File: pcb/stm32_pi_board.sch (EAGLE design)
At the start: 96 parts, among them IC1 MIC5219-3.3, IC2 ESP-11, IC3 IS31AP2005, IC4 STM32F405RG, IC5 STF203-22, IC6 MIC5219-3.3, IC7 IS31AP2005, IC8 MIC5219-3.3, IC9 UDA1334ATS, Q1 FDG6332C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

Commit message: New version of pi_board
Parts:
- removed ESPJ2: LSP10, MyComponents:LSP10
- removed IC1: MIC5219-3.3, MyComponents:MIC5219XX
- removed SV2: 75867-331LF, MyComponents:MA03-2
- added C38: 0.1uF, MyComponents:C-US0805
- added GN-RX-TX: (no value), MyComponents:MA03-1PL
- added IC10: REG1117, MyComponents:REG1117
- added L3: 1 uH, MyComponents:L-USL0805
- added R26, R27: 330, MyComponents:R-US0805
- added R28: 1, MyComponents:R-US0805
- C6: value 470pF -> 100 uF; device MyComponents:C-US0805 -> MyComponents:CPOL-US1311
- C7: value 2.2uF -> 47 uF
- D1: value WP154A4SUREQBFZGC -> (none); device MyComponents:RGB-LED-5MM -> MyComponents:RGB-LED3X1MM
- FLASH: value LSP10 -> (none); device MyComponents:LSP10 -> MyComponents:MA02-1
- HSE: device MyComponents:Q-HSEFA-128 -> MyComponents:Q-HSEHC-46X
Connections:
- removed net D1_BLUE: D1.AB, IC4MCU.PC2
- removed net D1_GREEN: D1.AG, IC4MCU.PC1
- removed net D1_RED: D1.AR, IC4MCU.PC3
- new net N$75: D1.AR, R27.1
- new net N$85: IC10.VOUT, R28.2
- new net N$90: L3.1, R28.1
- new net PC1: IC4MCU.PC1, SV3.6
- new net PC2: IC4MCU.PC2, SV3.5
- new net PC3: IC4MCU.PC3, SV3.4
- net ESP-IO0: now also FLASH.1; no longer FLASH.MP
- net ESP-RXI: now also GN-RX-TX.2; no longer SV2.5
- net ESP-TXI: now also GN-RX-TX.3; no longer SV2.3
- net GND: now also C38.2, C6.-, D1.C, FLASH.2, GN-RX-TX.1, IC10.GND; no longer C6.1, ESPJ2.MP, IC1.GND, R6.2, SV2.1
- net N$40: now also D1.AB, R26.1; no longer D1.C, R6.1
- net N$5: now also D1.AG, R6.1; no longer C6.2, IC1.BYP
- net PB4: now also R27.2; no longer SV3.11
- net PB5: now also R26.2; no longer SV3.10
- net PB6: now also SV3.11; no longer SV3.9
- net PB7: now also SV3.10; no longer SV3.8
- net PB8: now also R6.2; no longer SV3.7
- net PB9: now also SV3.9; no longer SV3.6
- net PC0: now also SV3.7; no longer SV3.4
- net PC13: now also SV3.8; no longer SV3.5
- net VDD: now also C6.+, L3.2; no longer IC1.OUT
- net VIN: now also C38.1, IC10.VIN; no longer IC1.EN, IC1.IN
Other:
- moved on the sheet: C10, C11, C12, C13, C14, C2, C3, C7, C8, C9, D1, ESP-ON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

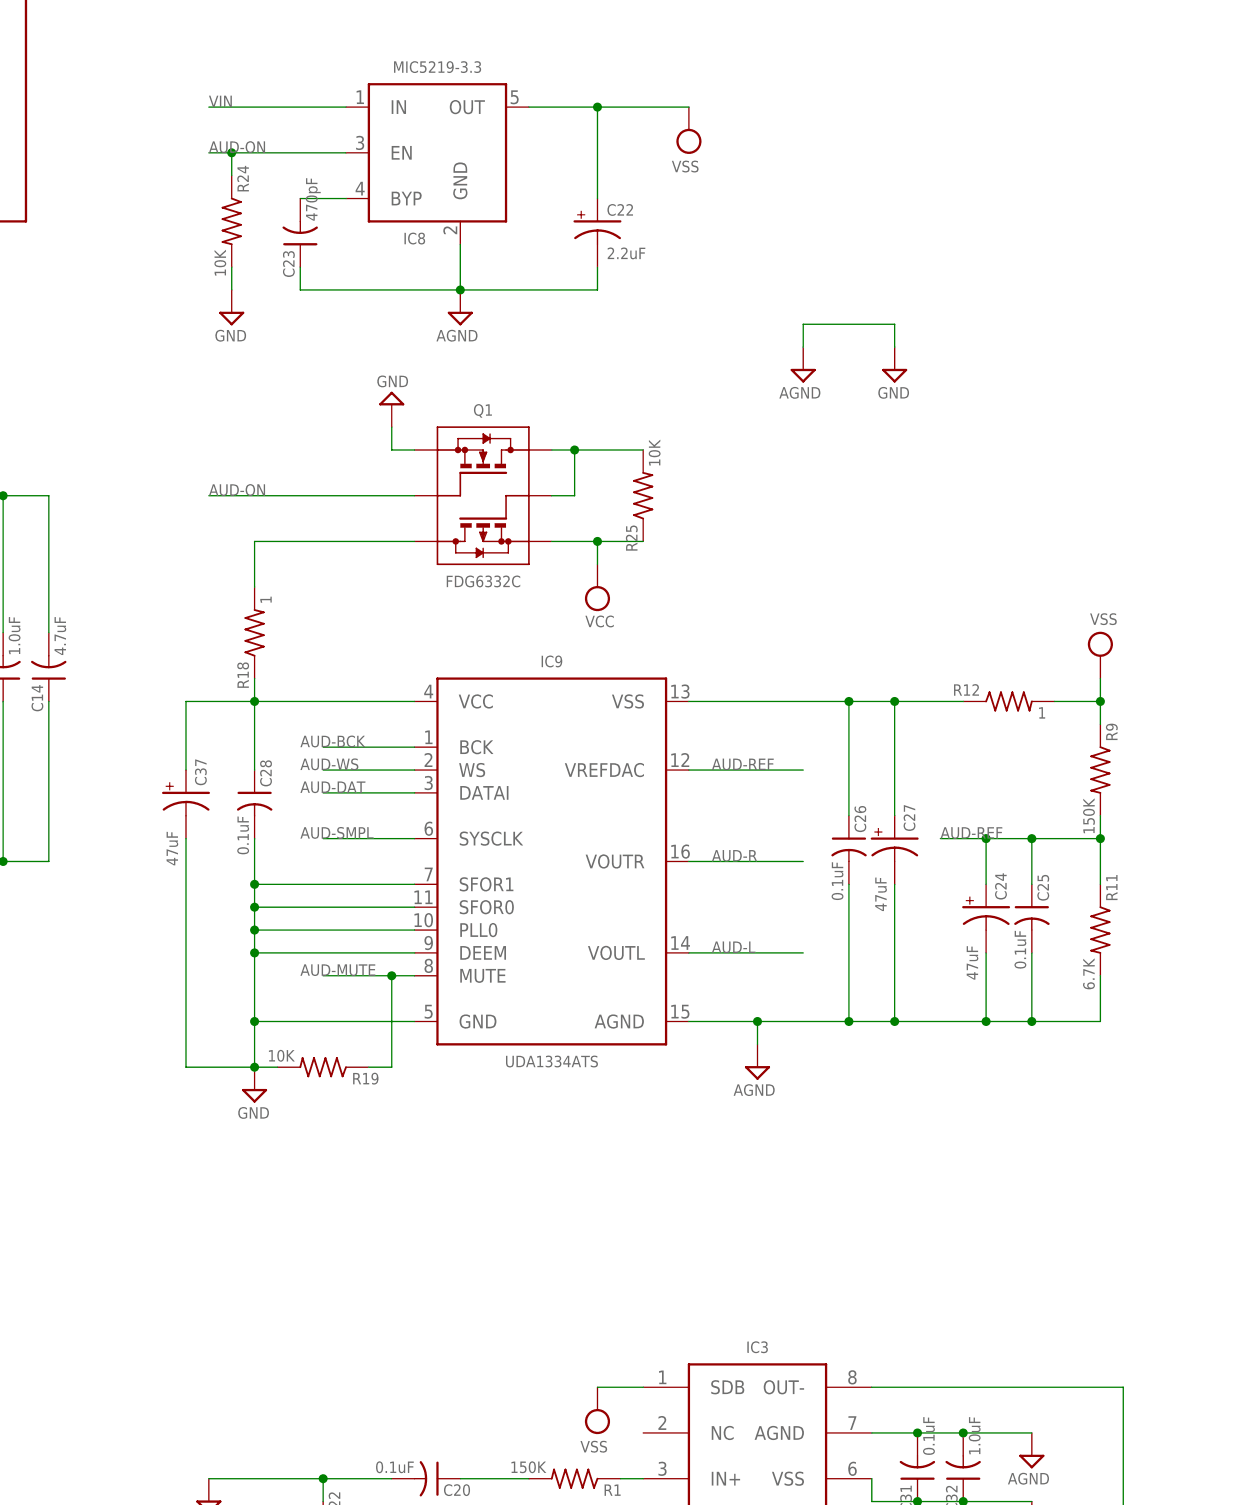
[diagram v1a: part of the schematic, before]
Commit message: Added LMT86
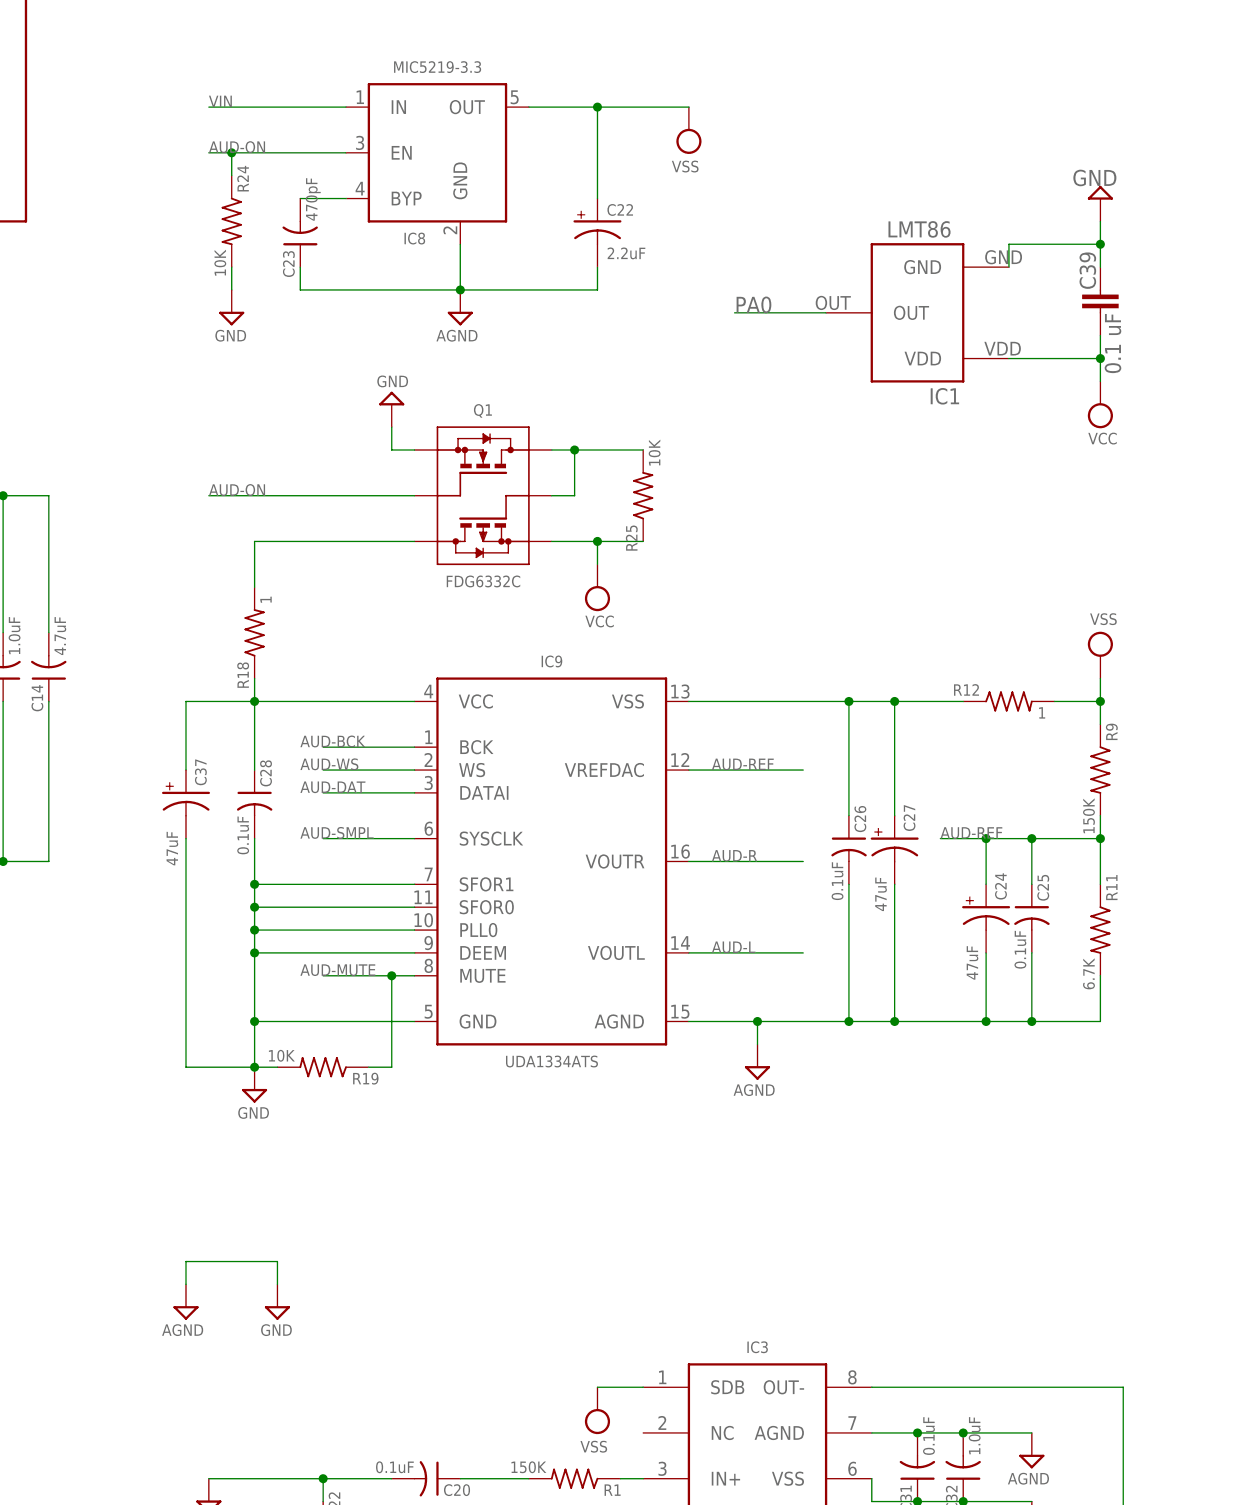
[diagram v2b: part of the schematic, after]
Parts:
- added C39: 0.1 uF, rcl:C-EUC1206
- added IC1: LMT86, MyComponents:LMT86
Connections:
- net GND: now also C39.1, IC1.GND
- net PA0: now also IC1.OUT
- net VDD: now also C39.2, IC1.VDD
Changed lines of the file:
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@@
 <part name="R27" library="MyComponents" deviceset="R-US" device="0805" value="330"/>
 <part name="R28" library="MyComponents" deviceset="R-US" device="0805" value="1"/>
+<part name="IC1" library="MyComponents" deviceset="LMT86" device=""/>
+<part name="SUPPLY19" library="supply2" deviceset="GND" device=""/>
+<part name="C39" library="rcl" deviceset="C-EU" device="C1206" value="0.1 uF"/>
+<part name="SUPPLY20" library="supply2" deviceset="VCC" device=""/>
 </parts>
 <sheets>
@@
 <attribute name="VALUE" x="314.325" y="12.065" size="1.27" layer="96" rot="R90" align="bottom-right"/>
 </instance>
-<instance part="SUPPLY13" gate="G$1" x="368.3" y="181.61" smashed="yes">
-<attribute name="VALUE" x="365.633" y="178.435" size="1.27" layer="96"/>
-</instance>
-<instance part="SUPPLY16" gate="GND" x="378.46" y="181.61" smashed="yes">
-<attribute name="VALUE" x="376.555" y="178.435" size="1.27" layer="96"/>
+<instance part="SUPPLY13" gate="G$1" x="299.72" y="77.47" smashed="yes">
+<attribute name="VALUE" x="297.053" y="74.295" size="1.27" layer="96"/>
+</instance>
+<instance part="SUPPLY16" gate="GND" x="309.88" y="77.47" smashed="yes">
+<attribute name="VALUE" x="307.975" y="74.295" size="1.27" layer="96"/>
 </instance>
 <instance part="Q1" gate="G$1" x="332.74" y="167.64" smashed="yes">
@@
 <attribute name="NAME" x="213.995" y="167.005" size="1.27" layer="95" rot="R180" align="bottom-right"/>
 <attribute name="VALUE" x="205.105" y="168.275" size="1.27" layer="96" align="bottom-right"/>
+</instance>
+<instance part="IC1" gate="G$1" x="381" y="187.96" rot="R180"/>
+<instance part="SUPPLY19" gate="GND" x="401.32" y="200.66" rot="R180"/>
+<instance part="C39" gate="G$1" x="401.32" y="190.5"/>
+<instance part="SUPPLY20" gate="G$1" x="401.32" y="177.8" smashed="yes" rot="R180">
+<attribute name="VALUE" x="403.225" y="174.625" size="1.27" layer="96" rot="R180"/>
 </instance>
 </instances>
@@
 <segment>
 <pinref part="SUPPLY13" gate="G$1" pin="AGND"/>
-<wire x1="368.3" y1="184.15" x2="368.3" y2="186.69" width="0.1524" layer="91"/>
+<wire x1="299.72" y1="80.01" x2="299.72" y2="82.55" width="0.1524" layer="91"/>
 <pinref part="SUPPLY16" gate="GND" pin="GND"/>
-<wire x1="368.3" y1="186.69" x2="378.46" y2="186.69" width="0.1524" layer="91"/>
-<wire x1="378.46" y1="186.69" x2="378.46" y2="184.15" width="0.1524" layer="91"/>
+<wire x1="299.72" y1="82.55" x2="309.88" y2="82.55" width="0.1524" layer="91"/>
+<wire x1="309.88" y1="82.55" x2="309.88" y2="80.01" width="0.1524" layer="91"/>
 </segment>
 <segment>
@@
 <wire x1="342.9" y1="236.22" x2="350.52" y2="236.22" width="0.1524" layer="91"/>
 <wire x1="350.52" y1="236.22" x2="350.52" y2="233.68" width="0.1524" layer="91"/>
+</segment>
+<segment>
+<pinref part="SUPPLY19" gate="GND" pin="GND"/>
+<wire x1="401.32" y1="198.12" x2="401.32" y2="195.58" width="0.1524" layer="91"/>
+<wire x1="401.32" y1="195.58" x2="391.16" y2="195.58" width="0.1524" layer="91"/>
+<pinref part="IC1" gate="G$1" pin="GND"/>
+<wire x1="391.16" y1="195.58" x2="391.16" y2="193.04" width="0.1524" layer="91"/>
+<pinref part="C39" gate="G$1" pin="1"/>
+<wire x1="401.32" y1="193.04" x2="401.32" y2="195.58" width="0.1524" layer="91"/>
+<junction x="401.32" y="195.58"/>
 </segment>
 </net>
@@
 <junction x="345.44" y="162.56"/>
 </segment>
+<segment>
+<pinref part="SUPPLY20" gate="G$1" pin="VCC"/>
+<pinref part="IC1" gate="G$1" pin="VDD"/>
+<wire x1="401.32" y1="180.34" x2="401.32" y2="182.88" width="0.1524" layer="91"/>
+<wire x1="401.32" y1="182.88" x2="391.16" y2="182.88" width="0.1524" layer="91"/>
+<pinref part="C39" gate="G$1" pin="2"/>
+<wire x1="401.32" y1="185.42" x2="401.32" y2="182.88" width="0.1524" layer="91"/>
+<junction x="401.32" y="182.88"/>
+</segment>
 </net>
 <net name="NRST" class="0">
@@
 <pinref part="SV3" gate="1" pin="3"/>
 </segment>
-</net>
+<segment>
+<pinref part="IC1" gate="G$1" pin="OUT"/>
+<wire x1="370.84" y1="187.96" x2="360.68" y2="187.96" width="0.1524" layer="91"/>
+<label x="360.68" y="187.96" size="1.778" layer="95"/>
+</segment>
+</net>
